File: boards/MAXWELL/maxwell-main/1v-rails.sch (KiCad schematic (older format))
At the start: 94 parts, among them Q1 SSM6N58NU, Q2 SSM6N58NU, U53 IAF12020A007V-003-R, U54 IAF12020A007V-003-R, U55 IAF12020A007V-003-R, U57 OKL-T/3-W12P-C, U58 OKL-T/3-W12P-C, U59 RT9088A, U64 RT9088A, U69 INA233, U70 INA233, U71 INA233, U72 INA233, U73 INA233

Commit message: Assigned footprints for all capacitors
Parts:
- C283, C297, C298, C299, C300, C301, C302, C303, C304, C305, C306, C307, C325, C326: footprint (none) -> azonenberg_pcb:EIA_1210_CAP_NOSILK
- C308, C309, C310, C311, C312, C313, C314, C315, C316, C317, C318, C319, C329, C330: footprint (none) -> azonenberg_pcb:EIA_1206_CAP_NOSILK
- C320, C321, C322, C333, C334, C393, C394, C395, C396, C397: footprint (none) -> azonenberg_pcb:EIA_0402_CAP_NOSILK
- C327, C328, C331, C332, C335, C336, C337, C375, C376, C378, C379, C380: footprint (none) -> azonenberg_pcb:EIA_0805_CAP_NOSILK
- C338, C377, C381: footprint (none) -> azonenberg_pcb:EIA_0603_CAP_NOSILK

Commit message: Continued assigning footprints. Done with everything up to and not including resistors.
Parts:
- Q1, Q2: footprint (none) -> azonenberg_pcb:DFN_6_0.65MM_2x2MM_GDS
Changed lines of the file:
@@
 F 0 "Q1" H 1794 10653 60  0000 L CNN
 F 1 "SSM6N58NU" H 1794 10547 60  0000 L CNN
-F 2 "" H 1650 10600 60  0001 C CNN
+F 2 "azonenberg_pcb:DFN_6_0.65MM_2x2MM_GDS" H 1650 10600 60  0001 C CNN
 F 3 "transistors/mos/*.*" H 1794 10494 60  0001 L CNN
 	1    1650 10600
@@
 F 0 "Q1" H 3394 10653 60  0000 L CNN
 F 1 "SSM6N58NU" H 3394 10547 60  0000 L CNN
-F 2 "" H 3250 10600 60  0001 C CNN
+F 2 "azonenberg_pcb:DFN_6_0.65MM_2x2MM_GDS" H 3250 10600 60  0001 C CNN
 F 3 "transistors/mos/*.*" H 3394 10494 60  0001 L CNN
 	2    3250 10600
@@
 F 0 "Q2" H 4994 10653 60  0000 L CNN
 F 1 "SSM6N58NU" H 4994 10547 60  0000 L CNN
-F 2 "" H 4850 10600 60  0001 C CNN
+F 2 "azonenberg_pcb:DFN_6_0.65MM_2x2MM_GDS" H 4850 10600 60  0001 C CNN
 F 3 "transistors/mos/*.*" H 4994 10494 60  0001 L CNN
 	1    4850 10600
@@
 F 0 "Q2" H 6594 10653 60  0000 L CNN
 F 1 "SSM6N58NU" H 6594 10547 60  0000 L CNN
-F 2 "" H 6450 10600 60  0001 C CNN
+F 2 "azonenberg_pcb:DFN_6_0.65MM_2x2MM_GDS" H 6450 10600 60  0001 C CNN
 F 3 "transistors/mos/*.*" H 6594 10494 60  0001 L CNN
 	2    6450 10600

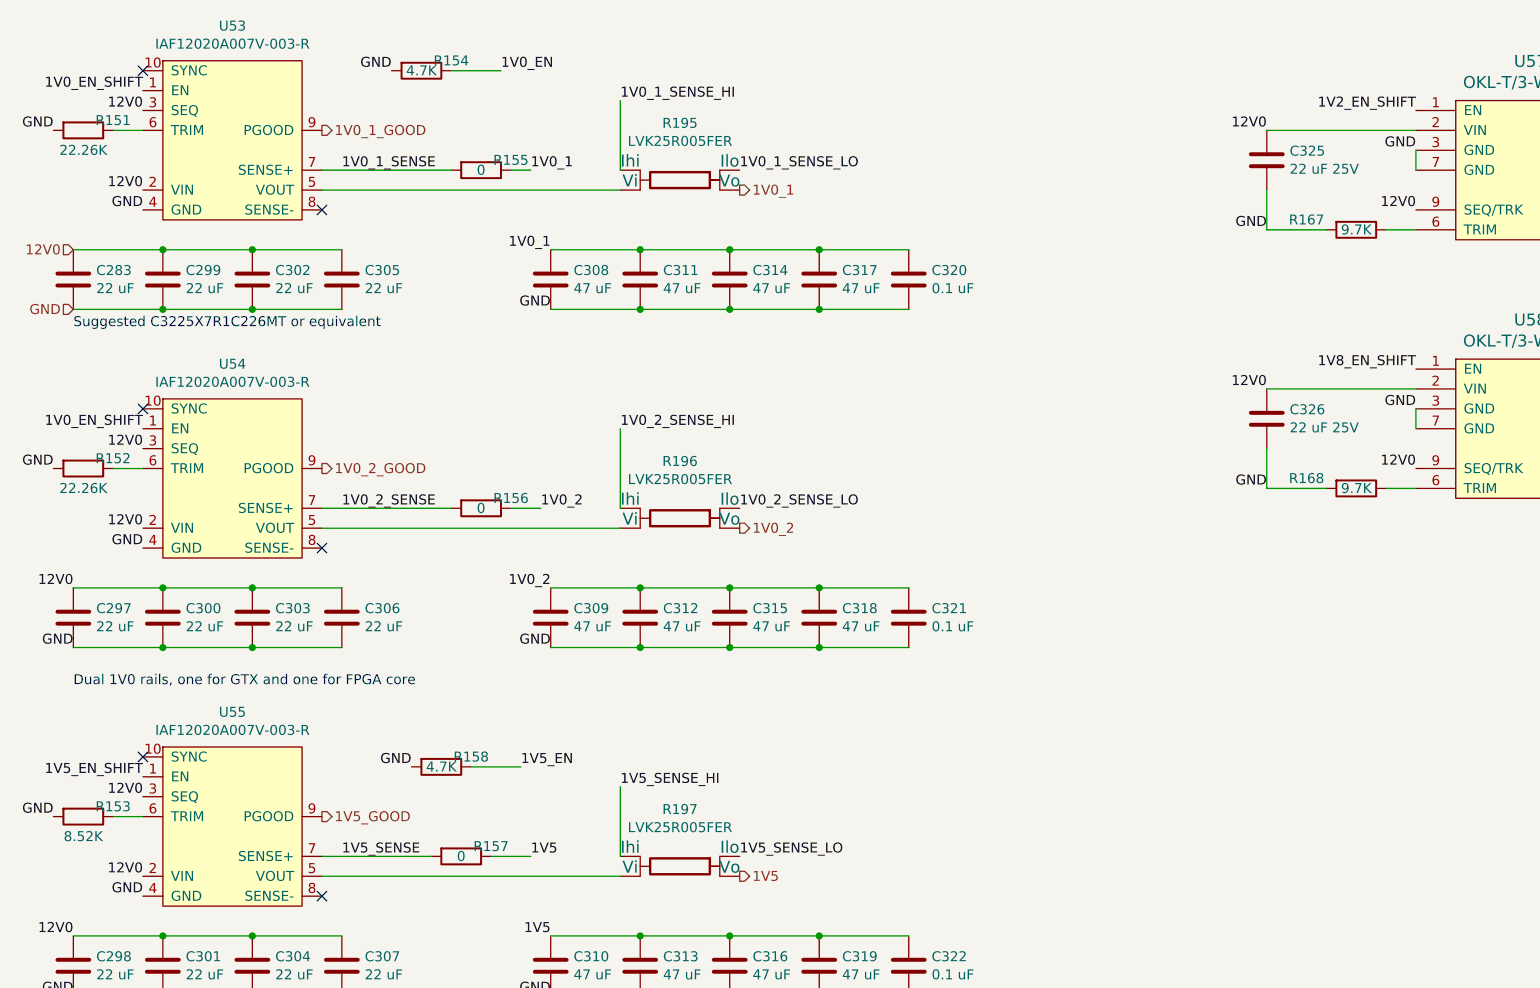
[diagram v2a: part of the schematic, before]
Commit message: Assigned footprints for all resistors
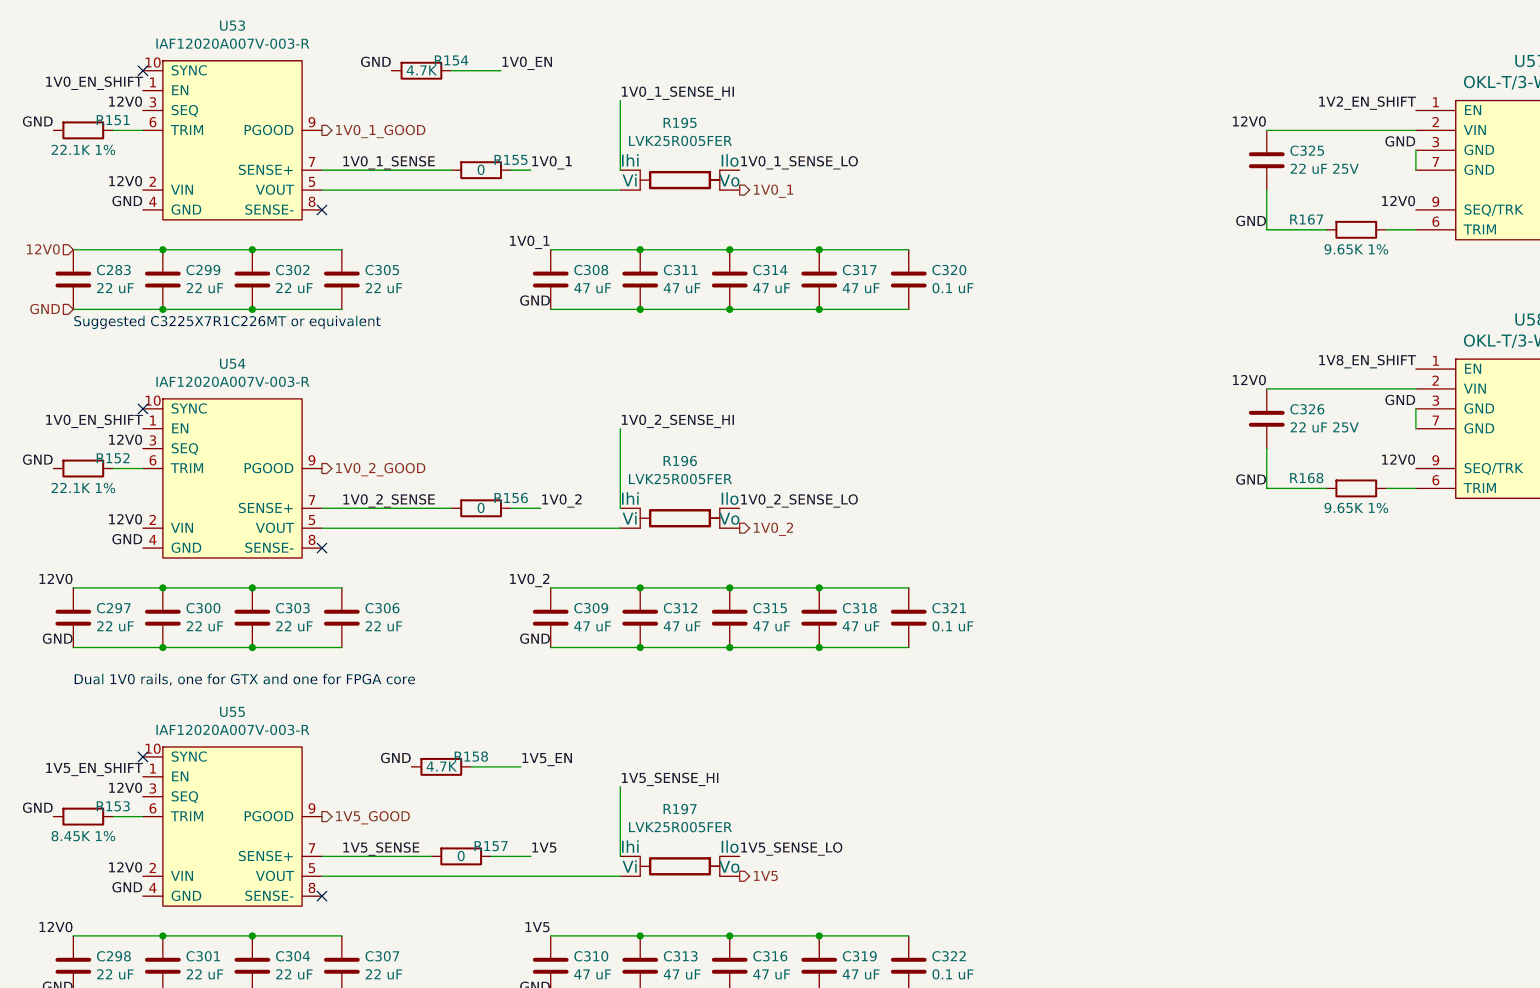
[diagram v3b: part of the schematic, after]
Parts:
- R151, R152: value 22.26K -> 22.1K 1%; footprint (none) -> azonenberg_pcb:EIA_0402_RES_NOSILK
- R153: value 8.52K -> 8.45K 1%; footprint (none) -> azonenberg_pcb:EIA_0402_RES_NOSILK
- R154, R155, R156, R157, R158, R159, R160, R161, R162, R163, R164, R165, R166, R169, R170, R186, R187: footprint (none) -> azonenberg_pcb:EIA_0402_RES_NOSILK
- R167, R168: value 9.7K -> 9.65K 1%; footprint (none) -> azonenberg_pcb:EIA_0402_RES_NOSILK
- R195, R196, R197: footprint (none) -> azonenberg_pcb:OHMITE_LVK25
- R198, R199: footprint (none) -> azonenberg_pcb:OHMITE_LVK12
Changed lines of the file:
@@
 Sheet 4 18
 Title "MAXWELL Main Board"
-Date "2020-06-22"
+Date "2020-06-23"
 Rev "0.1"
 Comp "Antikernel Labs"
@@
 F 0 "R155" V 3050 1500 50  0000 C CNN
 F 1 "0" V 3100 1350 50  0000 C CNN
-F 2 "" V 3030 1350 50  0001 C CNN
+F 2 "azonenberg_pcb:EIA_0402_RES_NOSILK" V 3030 1350 50  0001 C CNN
 F 3 "" H 3100 1350 50  0001 C CNN
 	1    3100 1350
@@
 F 0 "R154" V 2750 1000 50  0000 C CNN
 F 1 "4.7K" V 2800 850 50  0000 C CNN
-F 2 "" V 2730 850 50  0001 C CNN
+F 2 "azonenberg_pcb:EIA_0402_RES_NOSILK" V 2730 850 50  0001 C CNN
 F 3 "" H 2800 850 50  0001 C CNN
 	1    2800 850
@@
 AR Path="/5EDD7150/61296AEB/6129FB37" Ref="R151"  Part="1"
 F 0 "R151" V 1050 1300 50  0000 C CNN
-F 1 "22.26K" V 1200 1150 50  0000 C CNN
-F 2 "" V 1030 1150 50  0001 C CNN
+F 1 "22.1K 1%" V 1200 1150 50  0000 C CNN
+F 2 "azonenberg_pcb:EIA_0402_RES_NOSILK" V 1030 1150 50  0001 C CNN
 F 3 "" H 1100 1150 50  0001 C CNN
 	1    1100 1150
@@
 F 0 "R156" V 3050 3200 50  0000 C CNN
 F 1 "0" V 3100 3050 50  0000 C CNN
-F 2 "" V 3030 3050 50  0001 C CNN
+F 2 "azonenberg_pcb:EIA_0402_RES_NOSILK" V 3030 3050 50  0001 C CNN
 F 3 "" H 3100 3050 50  0001 C CNN
 	1    3100 3050
@@
 AR Path="/5EDD7150/61296AEB/6129FBAA" Ref="R152"  Part="1"
 F 0 "R152" V 1050 3000 50  0000 C CNN
-F 1 "22.26K" V 1200 2850 50  0000 C CNN
-F 2 "" V 1030 2850 50  0001 C CNN
+F 1 "22.1K 1%" V 1200 2850 50  0000 C CNN
+F 2 "azonenberg_pcb:EIA_0402_RES_NOSILK" V 1030 2850 50  0001 C CNN
 F 3 "" H 1100 2850 50  0001 C CNN
 	1    1100 2850
@@
 F 0 "R157" V 2950 4950 50  0000 C CNN
 F 1 "0" V 3000 4800 50  0000 C CNN
-F 2 "" V 2930 4800 50  0001 C CNN
+F 2 "azonenberg_pcb:EIA_0402_RES_NOSILK" V 2930 4800 50  0001 C CNN
 F 3 "" H 3000 4800 50  0001 C CNN
 	1    3000 4800
@@
 AR Path="/5EDD7150/61296AEB/612AEE23" Ref="R153"  Part="1"
 F 0 "R153" V 1050 4750 50  0000 C CNN
-F 1 "8.52K" V 1200 4600 50  0000 C CNN
-F 2 "" V 1030 4600 50  0001 C CNN
+F 1 "8.45K 1%" V 1200 4600 50  0000 C CNN
+F 2 "azonenberg_pcb:EIA_0402_RES_NOSILK" V 1030 4600 50  0001 C CNN
 F 3 "" H 1100 4600 50  0001 C CNN
 	1    1100 4600
@@
 F 0 "R158" V 2850 4500 50  0000 C CNN
 F 1 "4.7K" V 2900 4350 50  0000 C CNN
-F 2 "" V 2830 4350 50  0001 C CNN
+F 2 "azonenberg_pcb:EIA_0402_RES_NOSILK" V 2830 4350 50  0001 C CNN
 F 3 "" H 2900 4350 50  0001 C CNN
 	1    2900 4350
@@
 F 0 "R160" H 1820 10296 50  0000 L CNN
 F 1 "10K" H 1820 10205 50  0000 L CNN
-F 2 "" V 1680 10250 50  0001 C CNN
+F 2 "azonenberg_pcb:EIA_0402_RES_NOSILK" V 1680 10250 50  0001 C CNN
 F 3 "" H 1750 10250 50  0001 C CNN
 	1    1750 10250
@@
 F 0 "R159" H 1370 10296 50  0000 L CNN
 F 1 "10K" H 1370 10205 50  0000 L CNN
-F 2 "" V 1230 10250 50  0001 C CNN
+F 2 "azonenberg_pcb:EIA_0402_RES_NOSILK" V 1230 10250 50  0001 C CNN
 F 3 "" H 1300 10250 50  0001 C CNN
 	1    1300 10250
@@
 F 0 "R162" H 3420 10296 50  0000 L CNN
 F 1 "10K" H 3420 10205 50  0000 L CNN
-F 2 "" V 3280 10250 50  0001 C CNN
+F 2 "azonenberg_pcb:EIA_0402_RES_NOSILK" V 3280 10250 50  0001 C CNN
 F 3 "" H 3350 10250 50  0001 C CNN
 	1    3350 10250
@@
 F 0 "R161" H 2970 10296 50  0000 L CNN
 F 1 "10K" H 2970 10205 50  0000 L CNN
-F 2 "" V 2830 10250 50  0001 C CNN
+F 2 "azonenberg_pcb:EIA_0402_RES_NOSILK" V 2830 10250 50  0001 C CNN
 F 3 "" H 2900 10250 50  0001 C CNN
 	1    2900 10250
@@
 F 0 "R164" H 5020 10296 50  0000 L CNN
 F 1 "10K" H 5020 10205 50  0000 L CNN
-F 2 "" V 4880 10250 50  0001 C CNN
+F 2 "azonenberg_pcb:EIA_0402_RES_NOSILK" V 4880 10250 50  0001 C CNN
 F 3 "" H 4950 10250 50  0001 C CNN
 	1    4950 10250
@@
 F 0 "R163" H 4570 10296 50  0000 L CNN
 F 1 "10K" H 4570 10205 50  0000 L CNN
-F 2 "" V 4430 10250 50  0001 C CNN
+F 2 "azonenberg_pcb:EIA_0402_RES_NOSILK" V 4430 10250 50  0001 C CNN
 F 3 "" H 4500 10250 50  0001 C CNN
 	1    4500 10250
@@
 F 0 "R166" H 6620 10296 50  0000 L CNN
 F 1 "10K" H 6620 10205 50  0000 L CNN
-F 2 "" V 6480 10250 50  0001 C CNN
+F 2 "azonenberg_pcb:EIA_0402_RES_NOSILK" V 6480 10250 50  0001 C CNN
 F 3 "" H 6550 10250 50  0001 C CNN
 	1    6550 10250
@@
 F 0 "R165" H 6170 10296 50  0000 L CNN
 F 1 "10K" H 6170 10205 50  0000 L CNN
-F 2 "" V 6030 10250 50  0001 C CNN
+F 2 "azonenberg_pcb:EIA_0402_RES_NOSILK" V 6030 10250 50  0001 C CNN
 F 3 "" H 6100 10250 50  0001 C CNN
 	1    6100 10250
@@
 P 7500 1650
 F 0 "R167" V 7450 1400 50  0000 C CNN
-F 1 "9.7K" V 7500 1650 50  0000 C CNN
-F 2 "" V 7430 1650 50  0001 C CNN
+F 1 "9.65K 1%" V 7600 1650 50  0000 C CNN
+F 2 "azonenberg_pcb:EIA_0402_RES_NOSILK" V 7430 1650 50  0001 C CNN
 F 3 "" H 7500 1650 50  0001 C CNN
 	1    7500 1650
@@
 P 7500 2950
 F 0 "R168" V 7450 2700 50  0000 C CNN
-F 1 "9.7K" V 7500 2950 50  0000 C CNN
-F 2 "" V 7430 2950 50  0001 C CNN
+F 1 "9.65K 1%" V 7600 2950 50  0000 C CNN
+F 2 "azonenberg_pcb:EIA_0402_RES_NOSILK" V 7430 2950 50  0001 C CNN
 F 3 "" H 7500 2950 50  0001 C CNN
 	1    7500 2950
@@
 F 0 "R169" H 1320 6096 50  0000 L CNN
 F 1 "10K 1%" H 1320 6005 50  0000 L CNN
-F 2 "" V 1180 6050 50  0001 C CNN
+F 2 "azonenberg_pcb:EIA_0402_RES_NOSILK" V 1180 6050 50  0001 C CNN
 F 3 "" H 1250 6050 50  0001 C CNN
 	1    1250 6050
@@
 F 0 "R170" H 1320 6396 50  0000 L CNN
 F 1 "10K 1%" H 1320 6305 50  0000 L CNN
-F 2 "" V 1180 6350 50  0001 C CNN
+F 2 "azonenberg_pcb:EIA_0402_RES_NOSILK" V 1180 6350 50  0001 C CNN
 F 3 "" H 1250 6350 50  0001 C CNN
 	1    1250 6350
@@
 F 0 "R186" H 1320 7896 50  0000 L CNN
 F 1 "10K 1%" H 1320 7805 50  0000 L CNN
-F 2 "" V 1180 7850 50  0001 C CNN
+F 2 "azonenberg_pcb:EIA_0402_RES_NOSILK" V 1180 7850 50  0001 C CNN
 F 3 "" H 1250 7850 50  0001 C CNN
 	1    1250 7850
@@
 F 0 "R187" H 1320 8196 50  0000 L CNN
 F 1 "10K 1%" H 1320 8105 50  0000 L CNN
-F 2 "" V 1180 8150 50  0001 C CNN
+F 2 "azonenberg_pcb:EIA_0402_RES_NOSILK" V 1180 8150 50  0001 C CNN
 F 3 "" H 1250 8150 50  0001 C CNN
 	1    1250 8150
@@
 F 0 "R198" V 9714 1200 50  0000 C CNN
 F 1 "LVK12R012FER" V 9805 1200 50  0000 C CNN
-F 2 "" H 10000 1200 60  0001 C CNN
+F 2 "azonenberg_pcb:OHMITE_LVK12" H 10000 1200 60  0001 C CNN
 F 3 "" H 10000 1200 60  0000 C CNN
 	1    10000 1200
@@
 F 0 "R199" V 9714 2500 50  0000 C CNN
 F 1 "LVK12R012FER" V 9805 2500 50  0000 C CNN
-F 2 "" H 10000 2500 60  0001 C CNN
+F 2 "azonenberg_pcb:OHMITE_LVK12" H 10000 2500 60  0001 C CNN
 F 3 "" H 10000 2500 60  0000 C CNN
 	1    10000 2500
@@
 F 0 "R197" V 3814 4850 50  0000 C CNN
 F 1 "LVK25R005FER" V 3905 4850 50  0000 C CNN
-F 2 "" H 4100 4850 60  0001 C CNN
+F 2 "azonenberg_pcb:OHMITE_LVK25" H 4100 4850 60  0001 C CNN
 F 3 "" H 4100 4850 60  0000 C CNN
 	1    4100 4850
@@
 F 0 "R196" V 3814 3100 50  0000 C CNN
 F 1 "LVK25R005FER" V 3905 3100 50  0000 C CNN
-F 2 "" H 4100 3100 60  0001 C CNN
+F 2 "azonenberg_pcb:OHMITE_LVK25" H 4100 3100 60  0001 C CNN
 F 3 "" H 4100 3100 60  0000 C CNN
 	1    4100 3100
@@
 F 0 "R195" V 3814 1400 50  0000 C CNN
 F 1 "LVK25R005FER" V 3905 1400 50  0000 C CNN
-F 2 "" H 4100 1400 60  0001 C CNN
+F 2 "azonenberg_pcb:OHMITE_LVK25" H 4100 1400 60  0001 C CNN
 F 3 "" H 4100 1400 60  0000 C CNN
 	1    4100 1400

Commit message: Began assigning IC footprints
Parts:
- U69, U70, U71, U72, U73: footprint (none) -> azonenberg_pcb:SOP_10_0.5MM_3MM
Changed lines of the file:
@@
 F 0 "U69" H 13300 950 60  0000 C CNN
 F 1 "INA233" H 13700 950 60  0000 C CNN
-F 2 "" H 13400 1300 60  0001 C CNN
+F 2 "azonenberg_pcb:SOP_10_0.5MM_3MM" H 13400 1300 60  0001 C CNN
 F 3 "" H 13400 1300 60  0000 C CNN
 	1    13400 1300
@@
 F 0 "U70" H 13300 1800 60  0000 C CNN
 F 1 "INA233" H 13700 1800 60  0000 C CNN
-F 2 "" H 13400 2150 60  0001 C CNN
+F 2 "azonenberg_pcb:SOP_10_0.5MM_3MM" H 13400 2150 60  0001 C CNN
 F 3 "" H 13400 2150 60  0000 C CNN
 	1    13400 2150
@@
 F 0 "U71" H 13300 2650 60  0000 C CNN
 F 1 "INA233" H 13700 2650 60  0000 C CNN
-F 2 "" H 13400 3000 60  0001 C CNN
+F 2 "azonenberg_pcb:SOP_10_0.5MM_3MM" H 13400 3000 60  0001 C CNN
 F 3 "" H 13400 3000 60  0000 C CNN
 	1    13400 3000
@@
 F 0 "U72" H 13300 3500 60  0000 C CNN
 F 1 "INA233" H 13700 3500 60  0000 C CNN
-F 2 "" H 13400 3850 60  0001 C CNN
+F 2 "azonenberg_pcb:SOP_10_0.5MM_3MM" H 13400 3850 60  0001 C CNN
 F 3 "" H 13400 3850 60  0000 C CNN
 	1    13400 3850
@@
 F 0 "U73" H 13300 4350 60  0000 C CNN
 F 1 "INA233" H 13700 4350 60  0000 C CNN
-F 2 "" H 13400 4700 60  0001 C CNN
+F 2 "azonenberg_pcb:SOP_10_0.5MM_3MM" H 13400 4700 60  0001 C CNN
 F 3 "" H 13400 4700 60  0000 C CNN
 	1    13400 4700

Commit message: Added footprints for most ICs other than DC-DC modules
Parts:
- U57, U58: footprint (none) -> azonenberg_pcb:MODULE_MURATA_OKL-T3-W12
- U59, U64: footprint (none) -> azonenberg_pcb:DFN_10_0.5MM_3x3MM
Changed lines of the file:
@@
 F 0 "U57" H 8375 2597 60  0000 C CNN
 F 1 "OKL-T/3-W12P-C" H 8375 2491 60  0000 C CNN
-F 2 "" H 8000 1600 60  0001 C CNN
+F 2 "azonenberg_pcb:MODULE_MURATA_OKL-T3-W12" H 8000 1600 60  0001 C CNN
 F 3 "" H 8000 1600 60  0001 C CNN
 	1    8000 1700
@@
 F 0 "U58" H 8375 3897 60  0000 C CNN
 F 1 "OKL-T/3-W12P-C" H 8375 3791 60  0000 C CNN
-F 2 "" H 8000 2900 60  0001 C CNN
+F 2 "azonenberg_pcb:MODULE_MURATA_OKL-T3-W12" H 8000 2900 60  0001 C CNN
 F 3 "" H 8000 2900 60  0001 C CNN
 	1    8000 3000
@@
 F 0 "U59" H 2775 7825 50  0000 C CNN
 F 1 "RT9088A" H 2775 7734 50  0000 C CNN
-F 2 "" H 2300 6950 50  0001 C CNN
+F 2 "azonenberg_pcb:DFN_10_0.5MM_3x3MM" H 2300 6950 50  0001 C CNN
 F 3 "" H 2300 6950 50  0001 C CNN
 	1    2300 6850
@@
 F 0 "U64" H 2775 9625 50  0000 C CNN
 F 1 "RT9088A" H 2775 9534 50  0000 C CNN
-F 2 "" H 2300 8750 50  0001 C CNN
+F 2 "azonenberg_pcb:DFN_10_0.5MM_3x3MM" H 2300 8750 50  0001 C CNN
 F 3 "" H 2300 8750 50  0001 C CNN
 	1    2300 8650

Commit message: Added footprints for everything but LCD
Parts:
- U53, U54, U55: footprint (none) -> azonenberg_pcb:MODULE_DCDC_TDK_IAF
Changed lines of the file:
@@
 F 0 "U53" H 1850 2575 50  0000 C CNN
 F 1 "IAF12020A007V-003-R" H 1850 2484 50  0000 C CNN
-F 2 "" H 1500 1600 50  0001 C CNN
+F 2 "azonenberg_pcb:MODULE_DCDC_TDK_IAF" H 1500 1600 50  0001 C CNN
 F 3 "" H 1500 1600 50  0001 C CNN
 	1    1500 1600
@@
 F 0 "U54" H 1850 4275 50  0000 C CNN
 F 1 "IAF12020A007V-003-R" H 1850 4184 50  0000 C CNN
-F 2 "" H 1500 3300 50  0001 C CNN
+F 2 "azonenberg_pcb:MODULE_DCDC_TDK_IAF" H 1500 3300 50  0001 C CNN
 F 3 "" H 1500 3300 50  0001 C CNN
 	1    1500 3300
@@
 F 0 "U55" H 1850 6025 50  0000 C CNN
 F 1 "IAF12020A007V-003-R" H 1850 5934 50  0000 C CNN
-F 2 "" H 1500 5050 50  0001 C CNN
+F 2 "azonenberg_pcb:MODULE_DCDC_TDK_IAF" H 1500 5050 50  0001 C CNN
 F 3 "" H 1500 5050 50  0001 C CNN
 	1    1500 5050

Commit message: Continued schematic review
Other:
- note added: "1.xV rails are max 6A\nLVK25 are rated for 2W\n6A through 5 mR = 180 mW max"
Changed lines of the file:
@@
 NoConn ~ 12600 3850
 NoConn ~ 12600 4700
+Text Notes 6500 4050 0    50   ~ 0
+1.xV rails are max 6A\nLVK25 are rated for 2W\n6A through 5 mR = 180 mW max
 $EndSCHEMATC
